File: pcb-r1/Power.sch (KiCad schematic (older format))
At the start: 10 parts

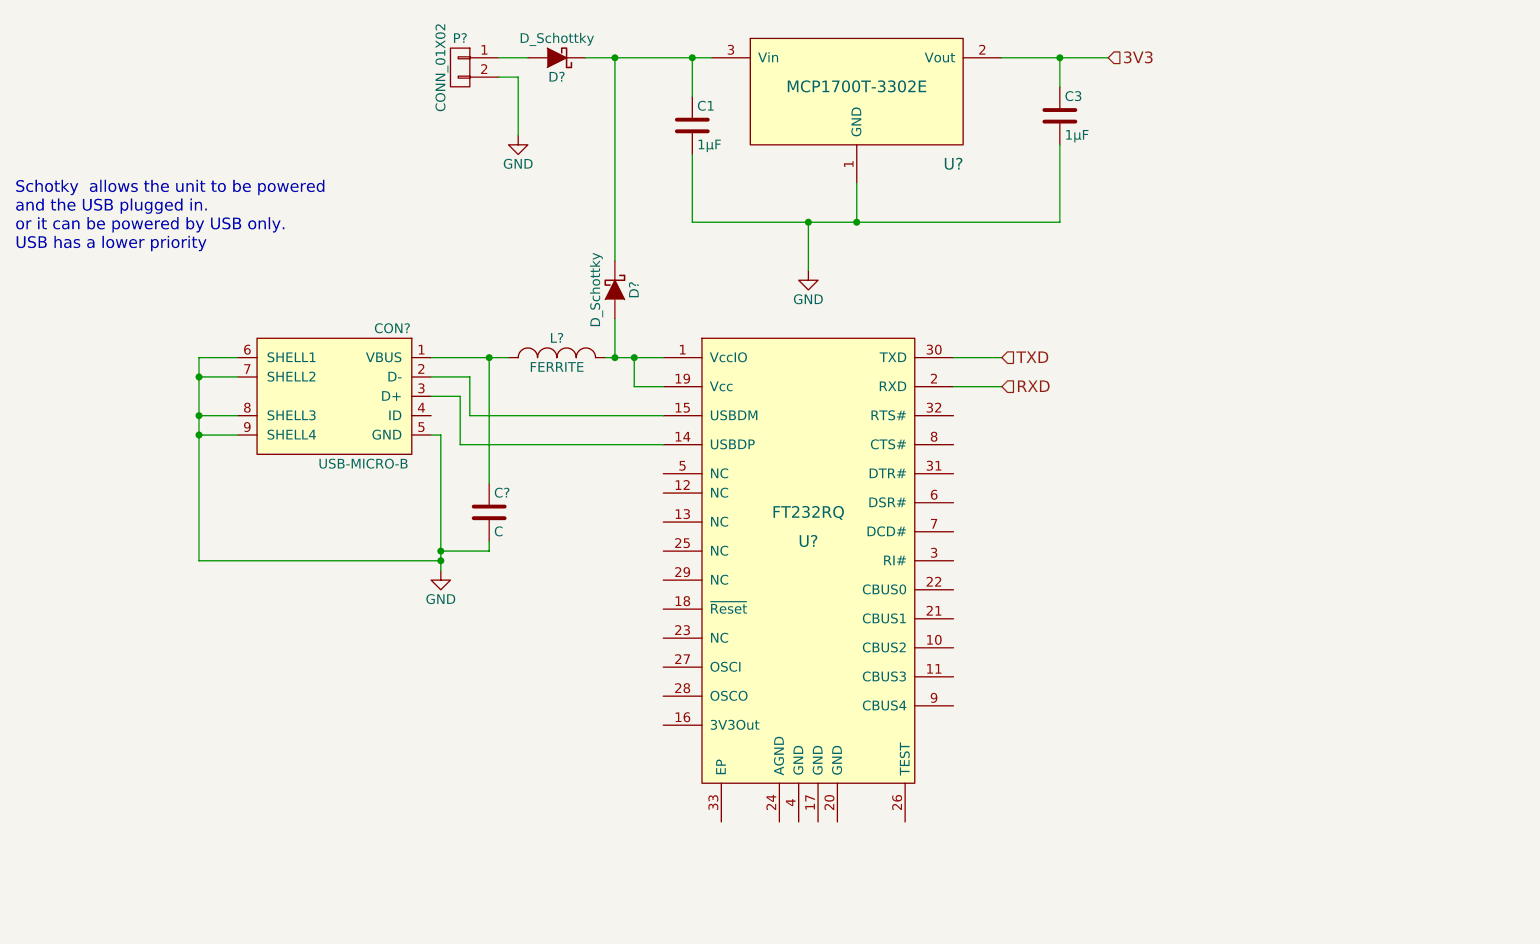
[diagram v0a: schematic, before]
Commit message: Added further enhancements to the power block
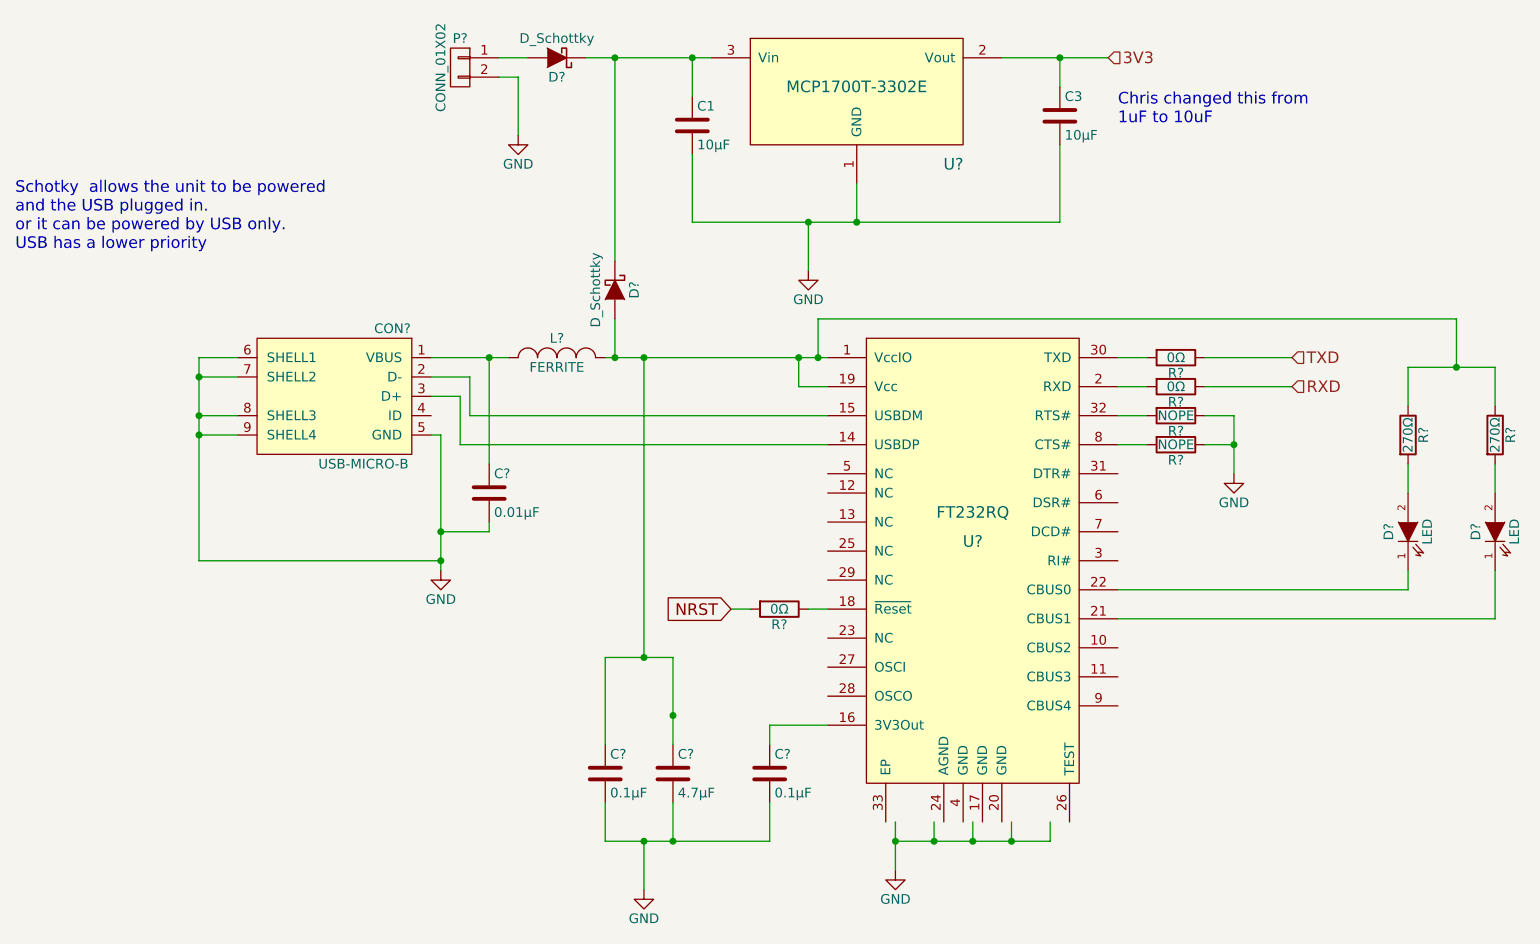
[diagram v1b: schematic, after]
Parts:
- added C? (x2): 0.1μF, symbol C
- added C?: 4.7μF, symbol C
- added D? (x2): LED, symbol LED
- added R? (x3): 0Ω, symbol R
- added R? (x2): 270Ω, symbol R
- added R? (x2): NOPE, symbol R
- C1, C3: value 1μF -> 10μF
- C?: value C -> 0.01μF
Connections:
- net labels added: NRST
- wire segments 37 -> 75
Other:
- note added: "Chris changed this from \n1uF to 10uF"
- moved on the sheet: C?, U?

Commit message: Updated the schematic with the latest from CC17
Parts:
- renumbered C3 to C?, C1 to C?
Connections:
- net labels added: PWR
- net labels removed: 3V3
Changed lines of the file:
@@
 $Descr A4 11693 8268
 encoding utf-8
-Sheet 2 2
+Sheet 2 3
 Title ""
 Date ""
@@
 $EndComp
 $Comp
-L C C3
+L C C?
 U 1 1 5657EDC1
 P 6400 3250
-F 0 "C3" H 6425 3350 50  0000 L CNN
+F 0 "C?" H 6425 3350 50  0000 L CNN
 F 1 "10μF" H 6425 3150 50  0000 L CNN
 F 2 "Capacitors_SMD:C_0805" H 6438 3100 30  0001 C CNN
@@
 $EndComp
 $Comp
-L C C1
+L C C?
 U 1 1 5657EDC8
 P 4500 3300
-F 0 "C1" H 4525 3400 50  0000 L CNN
+F 0 "C?" H 4525 3400 50  0000 L CNN
 F 1 "10μF" H 4525 3200 50  0000 L CNN
 F 2 "Capacitors_SMD:C_0805" H 4538 3150 30  0001 C CNN
@@
 $EndComp
 Text HLabel 6650 2950 2    60   Input ~ 0
-3V3
+PWR
 $Comp
 L C C?
@@
 	6400 3800 6400 3400
 Wire Wire Line
-	4500 3800 6400 3800
+	4500 3800 6700 3800
 Wire Wire Line
 	5350 3600 5350 3800
@@
 Wire Wire Line
 	6700 4650 6850 4650
+Text HLabel 6700 3800 2    60   Input ~ 0
+GND
+Connection ~ 6400 3800
 $EndSCHEMATC

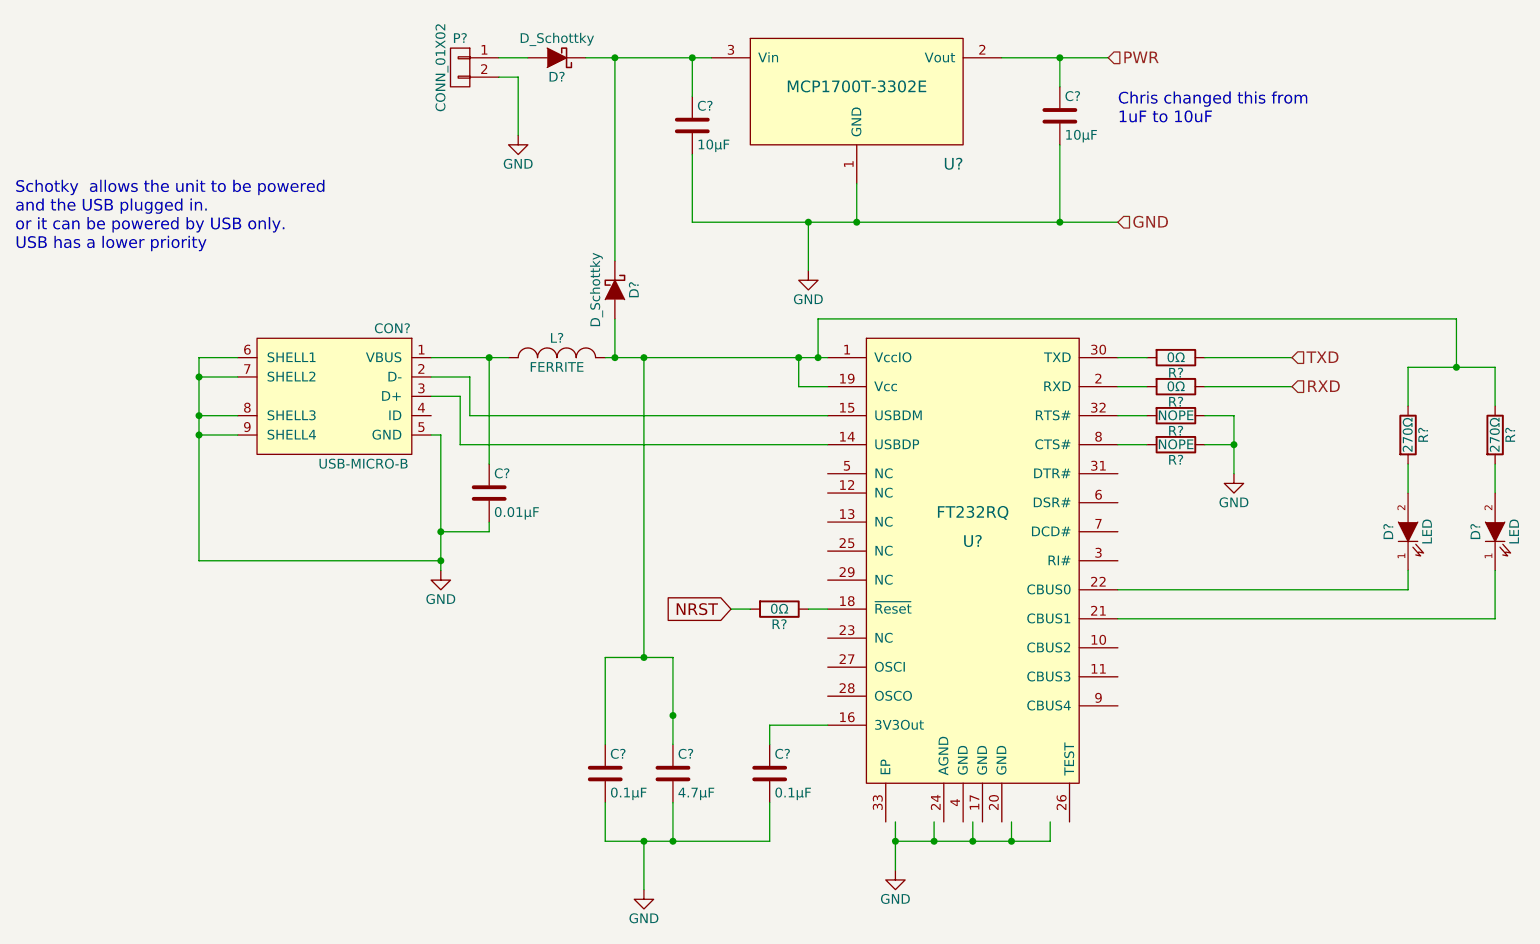
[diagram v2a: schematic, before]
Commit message: Edited the Central-Command.sch and forced the order of the hierarchical sheets to match the reference schematic annotations. Also annotated
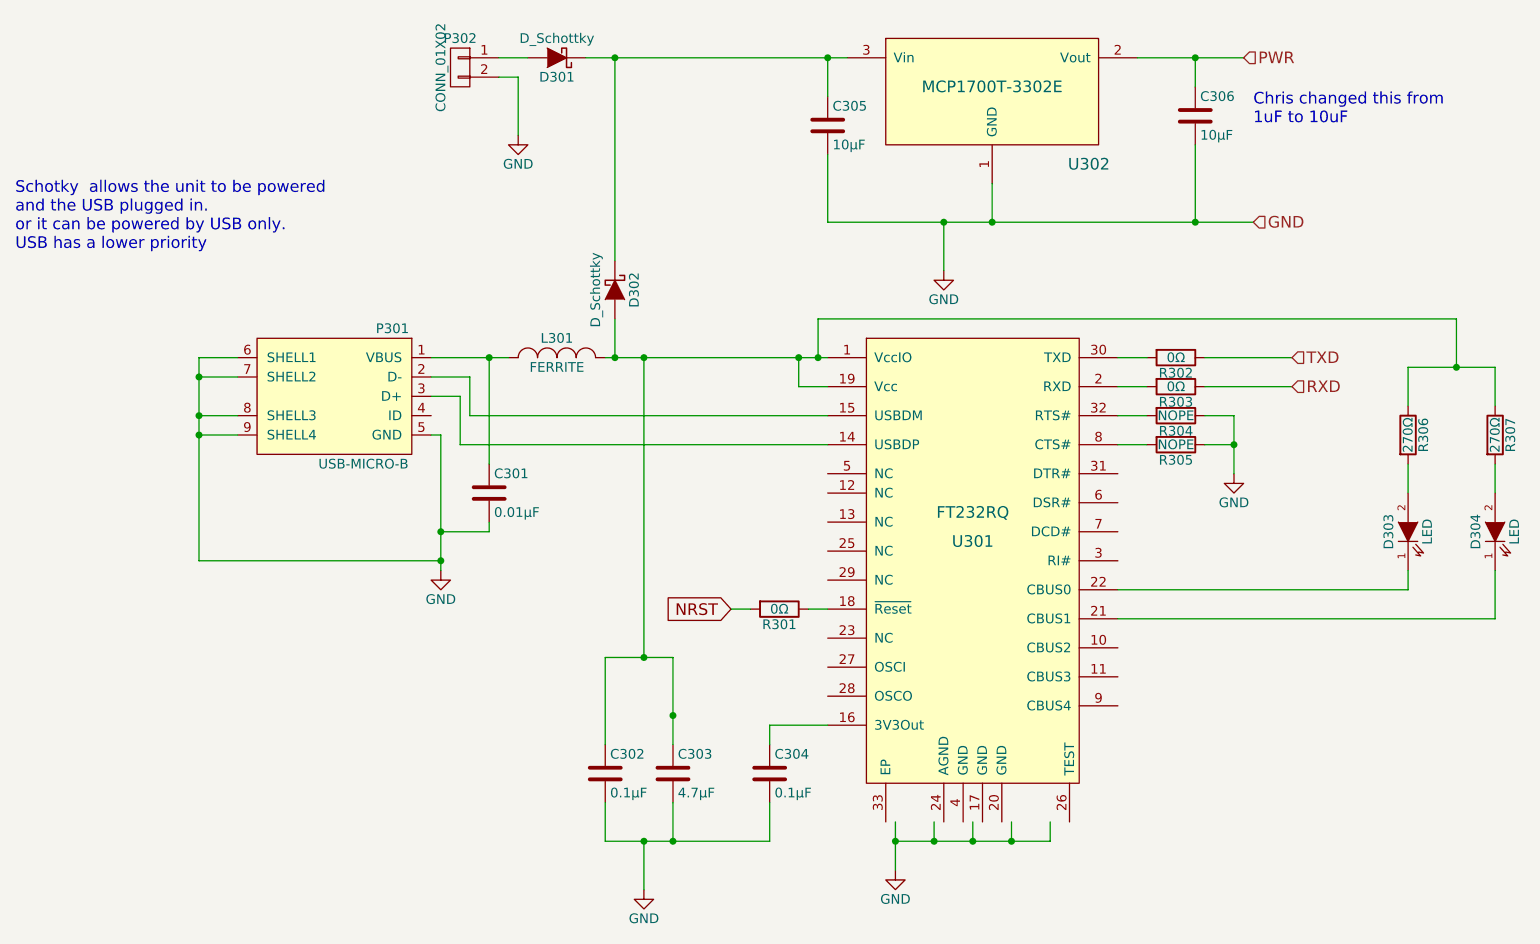
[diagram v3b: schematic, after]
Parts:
- gave numbers to parts that had none: 22
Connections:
- wire segments 75 -> 101
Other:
- moved on the sheet: C305, C306, U302

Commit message: Started the part to footprint association
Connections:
- wire segments 101 -> 75
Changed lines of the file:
@@
 $EndComp
 $Comp
-L GND #PWR305
+L GND #PWR010
 U 1 1 5657EDD1
 P 5800 4050
-F 0 "#PWR305" H 5800 3800 50  0001 C CNN
+F 0 "#PWR010" H 5800 3800 50  0001 C CNN
 F 1 "GND" H 5800 3900 50  0000 C CNN
 F 2 "" H 5800 4050 60  0000 C CNN
@@
 F 0 "P302" H 3300 3150 50  0000 C CNN
 F 1 "CONN_01X02" V 3400 3000 50  0000 C CNN
-F 2 "" H 3300 3000 60  0000 C CNN
+F 2 "" H 3300 3000 60  0001 C CNN
 F 3 "" H 3300 3000 60  0000 C CNN
 	1    3300 3000
@@
 $EndComp
 $Comp
-L GND #PWR302
+L GND #PWR011
 U 1 1 5657F45C
 P 3600 3350
-F 0 "#PWR302" H 3600 3100 50  0001 C CNN
+F 0 "#PWR011" H 3600 3100 50  0001 C CNN
 F 1 "GND" H 3600 3200 50  0000 C CNN
 F 2 "" H 3600 3350 60  0000 C CNN
@@
 F 0 "U301" H 5950 5350 60  0000 C CNN
 F 1 "FT232RQ" H 5950 5500 60  0000 C CNN
-F 2 "" H 5650 6000 60  0000 C CNN
+F 2 "" H 5650 6000 60  0001 C CNN
 F 3 "http://www.ftdichip.com/Support/Documents/DataSheets/ICs/DS_FT232R.pdf" H 5650 6000 60  0001 C CNN
 	1    5950 5400
@@
 F 0 "P301" H 2350 5050 50  0000 C CNN
 F 1 "USB-MICRO-B" H 2500 4350 50  0000 C CNN
-F 2 "" H 2650 4600 50  0000 C CNN
+F 2 "" H 2650 4600 50  0001 C CNN
 F 3 "" H 2650 4600 50  0000 C CNN
 	1    2650 4700
@@
 F 0 "L301" H 3800 4600 50  0000 C CNN
 F 1 "FERRITE" H 3800 4450 50  0000 C CNN
-F 2 "" H 3800 4500 60  0000 C CNN
+F 2 "" H 3800 4500 60  0001 C CNN
 F 3 "" H 3800 4500 60  0000 C CNN
 	1    3800 4500
@@
 F 0 "C301" H 3475 5300 50  0000 L CNN
 F 1 "0.01μF" H 3475 5100 50  0000 L CNN
-F 2 "" H 3488 5050 30  0000 C CNN
+F 2 "" H 3488 5050 30  0001 C CNN
 F 3 "" H 3450 5200 60  0000 C CNN
 	1    3450 5200
@@
 $EndComp
 $Comp
-L GND #PWR301
+L GND #PWR012
 U 1 1 565817D5
 P 3200 5600
-F 0 "#PWR301" H 3200 5350 50  0001 C CNN
+F 0 "#PWR012" H 3200 5350 50  0001 C CNN
 F 1 "GND" H 3200 5450 50  0000 C CNN
 F 2 "" H 3200 5600 60  0000 C CNN
@@
 F 0 "D301" H 3800 3050 50  0000 C CNN
 F 1 "D_Schottky" H 3800 2850 50  0000 C CNN
-F 2 "" H 3800 2950 60  0000 C CNN
+F 2 "" H 3800 2950 60  0001 C CNN
 F 3 "" H 3800 2950 60  0000 C CNN
 	1    3800 2950
@@
 F 0 "D302" H 4100 4250 50  0000 C CNN
 F 1 "D_Schottky" H 4100 4050 50  0000 C CNN
-F 2 "" H 4100 4150 60  0000 C CNN
+F 2 "" H 4100 4150 60  0001 C CNN
 F 3 "" H 4100 4150 60  0000 C CNN
 	1    4100 4150
@@
 F 0 "C302" H 4075 6750 50  0000 L CNN
 F 1 "0.1μF" H 4075 6550 50  0000 L CNN
-F 2 "" H 4088 6500 30  0000 C CNN
+F 2 "" H 4088 6500 30  0001 C CNN
 F 3 "" H 4050 6650 60  0000 C CNN
 	1    4050 6650
@@
 F 0 "C303" H 4425 6750 50  0000 L CNN
 F 1 "4.7μF" H 4425 6550 50  0000 L CNN
-F 2 "" H 4438 6500 30  0000 C CNN
+F 2 "" H 4438 6500 30  0001 C CNN
 F 3 "" H 4400 6650 60  0000 C CNN
 	1    4400 6650
@@
 $EndComp
 $Comp
-L GND #PWR303
+L GND #PWR013
 U 1 1 5659E477
 P 4250 7250
-F 0 "#PWR303" H 4250 7000 50  0001 C CNN
+F 0 "#PWR013" H 4250 7000 50  0001 C CNN
 F 1 "GND" H 4250 7100 50  0000 C CNN
 F 2 "" H 4250 7250 60  0000 C CNN
@@
 F 0 "C304" H 4925 6750 50  0000 L CNN
 F 1 "0.1μF" H 4925 6550 50  0000 L CNN
-F 2 "" H 4938 6500 30  0000 C CNN
+F 2 "" H 4938 6500 30  0001 C CNN
 F 3 "" H 4900 6650 60  0000 C CNN
 	1    4900 6650
@@
 F 0 "R301" V 5030 5800 50  0000 C CNN
 F 1 "0Ω" V 4950 5800 50  0000 C CNN
-F 2 "" V 4880 5800 30  0000 C CNN
+F 2 "" V 4880 5800 30  0001 C CNN
 F 3 "" H 4950 5800 30  0000 C CNN
 	1    4950 5800
@@
 $EndComp
 $Comp
-L GND #PWR304
+L GND #PWR014
 U 1 1 5659F562
 P 5550 7150
-F 0 "#PWR304" H 5550 6900 50  0001 C CNN
+F 0 "#PWR014" H 5550 6900 50  0001 C CNN
 F 1 "GND" H 5550 7000 50  0000 C CNN
 F 2 "" H 5550 7150 60  0000 C CNN
@@
 F 0 "R306" V 8280 4900 50  0000 C CNN
 F 1 "270Ω" V 8200 4900 50  0000 C CNN
-F 2 "" V 8130 4900 30  0000 C CNN
+F 2 "" V 8130 4900 30  0001 C CNN
 F 3 "" H 8200 4900 30  0000 C CNN
 	1    8200 4900
@@
 F 0 "D303" H 8200 5500 50  0000 C CNN
 F 1 "LED" H 8200 5300 50  0000 C CNN
-F 2 "" H 8200 5400 60  0000 C CNN
+F 2 "" H 8200 5400 60  0001 C CNN
 F 3 "" H 8200 5400 60  0000 C CNN
 	1    8200 5400
@@
 F 0 "R307" V 8730 4900 50  0000 C CNN
 F 1 "270Ω" V 8650 4900 50  0000 C CNN
-F 2 "" V 8580 4900 30  0000 C CNN
+F 2 "" V 8580 4900 30  0001 C CNN
 F 3 "" H 8650 4900 30  0000 C CNN
 	1    8650 4900
@@
 F 0 "D304" H 8650 5500 50  0000 C CNN
 F 1 "LED" H 8650 5300 50  0000 C CNN
-F 2 "" H 8650 5400 60  0000 C CNN
+F 2 "" H 8650 5400 60  0001 C CNN
 F 3 "" H 8650 5400 60  0000 C CNN
 	1    8650 5400
@@
 $EndComp
 Wire Wire Line
-	6800 2950 7100 2950
-Wire Wire Line
-	7100 2950 7350 2950
+	6800 2950 7350 2950
 Wire Wire Line
 	7100 2950 7100 3100
@@
 	7100 3800 7100 3400
 Wire Wire Line
-	5200 3800 5800 3800
-Wire Wire Line
-	5800 3800 6050 3800
-Wire Wire Line
-	6050 3800 7100 3800
-Wire Wire Line
-	7100 3800 7400 3800
+	5200 3800 7400 3800
 Wire Wire Line
 	6050 3600 6050 3800
@@
 	3600 3050 3600 3350
 Wire Wire Line
-	4050 4500 4100 4500
-Wire Wire Line
-	4100 4500 4250 4500
-Wire Wire Line
-	4250 4500 5050 4500
-Wire Wire Line
-	5050 4500 5150 4500
-Wire Wire Line
-	5150 4500 5200 4500
+	4050 4500 5200 4500
 Wire Wire Line
 	5050 4500 5050 4650
@@
 Connection ~ 5050 4500
 Wire Wire Line
-	3150 4500 3450 4500
-Wire Wire Line
-	3450 4500 3550 4500
+	3150 4500 3550 4500
 Wire Wire Line
 	3450 4500 3450 5050
@@
 	3150 4900 3200 4900
 Wire Wire Line
-	3200 4900 3200 5400
-Wire Wire Line
-	3200 5400 3200 5550
-Wire Wire Line
-	3200 5550 3200 5600
+	3200 4900 3200 5600
 Wire Wire Line
 	2150 4500 1950 4500
 Wire Wire Line
-	1950 4500 1950 4600
-Wire Wire Line
-	1950 4600 1950 4800
-Wire Wire Line
-	1950 4800 1950 4900
-Wire Wire Line
-	1950 4900 1950 5550
+	1950 4500 1950 5550
 Wire Wire Line
 	1950 5550 3200 5550
@@
 	3500 2950 3650 2950
 Wire Wire Line
-	3950 2950 4100 2950
-Wire Wire Line
-	4100 2950 5200 2950
-Wire Wire Line
-	5200 2950 5300 2950
+	3950 2950 5300 2950
 Wire Wire Line
 	4050 6050 4050 6500
 Wire Wire Line
-	4050 6050 4250 6050
-Wire Wire Line
-	4250 6050 4400 6050
-Wire Wire Line
-	4400 6050 4400 6350
-Wire Wire Line
-	4400 6350 4400 6500
+	4050 6050 4400 6050
+Wire Wire Line
+	4400 6050 4400 6500
 Wire Wire Line
 	4050 6800 4050 7000
 Wire Wire Line
-	4050 7000 4250 7000
-Wire Wire Line
-	4250 7000 4400 7000
-Wire Wire Line
-	4400 7000 4900 7000
+	4050 7000 4900 7000
 Wire Wire Line
 	4400 7000 4400 6800
@@
 	5100 5800 5200 5800
 Wire Wire Line
-	5550 6900 5550 7000
-Wire Wire Line
-	5550 7000 5550 7150
-Wire Wire Line
-	5550 7000 5750 7000
-Wire Wire Line
-	5750 7000 5950 7000
-Wire Wire Line
-	5950 7000 6150 7000
-Wire Wire Line
-	6150 7000 6350 7000
+	5550 6900 5550 7150
+Wire Wire Line
+	5550 7000 6350 7000
 Wire Wire Line
 	6350 7000 6350 6900
@@
 	8200 4750 8200 4550
 Wire Wire Line
-	8200 4550 8450 4550
-Wire Wire Line
-	8450 4550 8650 4550
+	8200 4550 8650 4550
 Wire Wire Line
 	8650 4550 8650 4750
@@
 F 0 "R304" V 7080 4800 50  0000 C CNN
 F 1 "NOPE" V 7000 4800 50  0000 C CNN
-F 2 "" V 6930 4800 30  0000 C CNN
+F 2 "" V 6930 4800 30  0001 C CNN
 F 3 "" H 7000 4800 30  0000 C CNN
 	1    7000 4800
@@
 F 0 "R305" V 7080 4950 50  0000 C CNN
 F 1 "NOPE" V 7000 4950 50  0000 C CNN
-F 2 "" V 6930 4950 30  0000 C CNN
+F 2 "" V 6930 4950 30  0001 C CNN
 F 3 "" H 7000 4950 30  0000 C CNN
 	1    7000 4950
@@
 	7150 4800 7300 4800
 Wire Wire Line
-	7300 4800 7300 4950
-Wire Wire Line
-	7300 4950 7300 5100
+	7300 4800 7300 5100
 Wire Wire Line
 	7300 4950 7150 4950
 $Comp
-L GND #PWR306
+L GND #PWR015
 U 1 1 565A0941
 P 7300 5100
-F 0 "#PWR306" H 7300 4850 50  0001 C CNN
+F 0 "#PWR015" H 7300 4850 50  0001 C CNN
 F 1 "GND" H 7300 4950 50  0000 C CNN
 F 2 "" H 7300 5100 60  0000 C CNN
@@
 F 0 "R302" V 7080 4500 50  0000 C CNN
 F 1 "0Ω" V 7000 4500 50  0000 C CNN
-F 2 "" V 6930 4500 30  0000 C CNN
+F 2 "" V 6930 4500 30  0001 C CNN
 F 3 "" H 7000 4500 30  0000 C CNN
 	1    7000 4500
@@
 F 0 "R303" V 7080 4650 50  0000 C CNN
 F 1 "0Ω" V 7000 4650 50  0000 C CNN
-F 2 "" V 6930 4650 30  0000 C CNN
+F 2 "" V 6930 4650 30  0001 C CNN
 F 3 "" H 7000 4650 30  0000 C CNN
 	1    7000 4650
